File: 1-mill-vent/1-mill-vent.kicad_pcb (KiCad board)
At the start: 2 copper layers, 96.5 x 55.9 mm, 60 parts, among them J1 Differential:/Single, J3 No_Power_Control, J4 Front_panel_control, J5 Fan, J6 Ext Parts, J7 EXT Power Option, J8 POWER, Q1 2N3904, Q2 2N3904, Q3 2N3904, Q4 TSM480p06, U1 LM358, U2 LM78L05_TO92, U3 TSR_1-24120, U4 MPXV

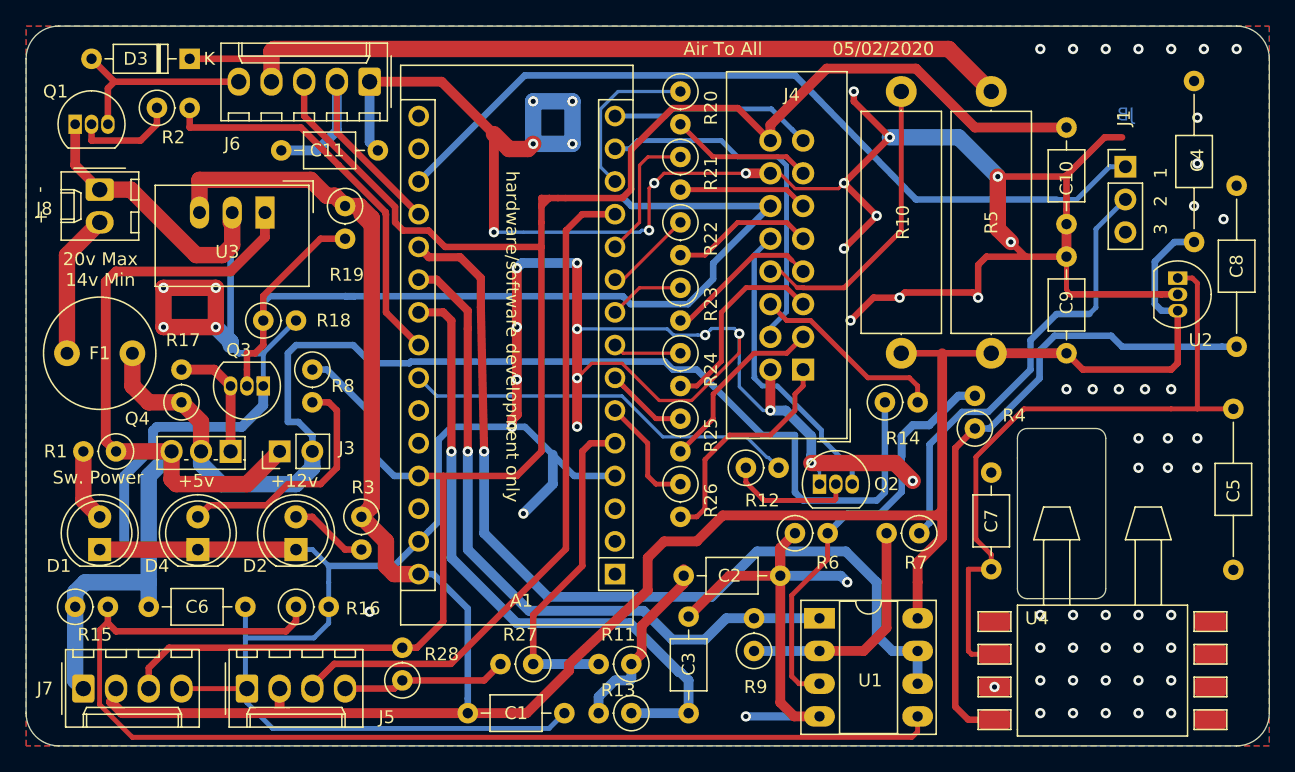
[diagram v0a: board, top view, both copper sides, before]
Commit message: Last update to ver1, start v2
V1 is first board
V2 is start of SMD design
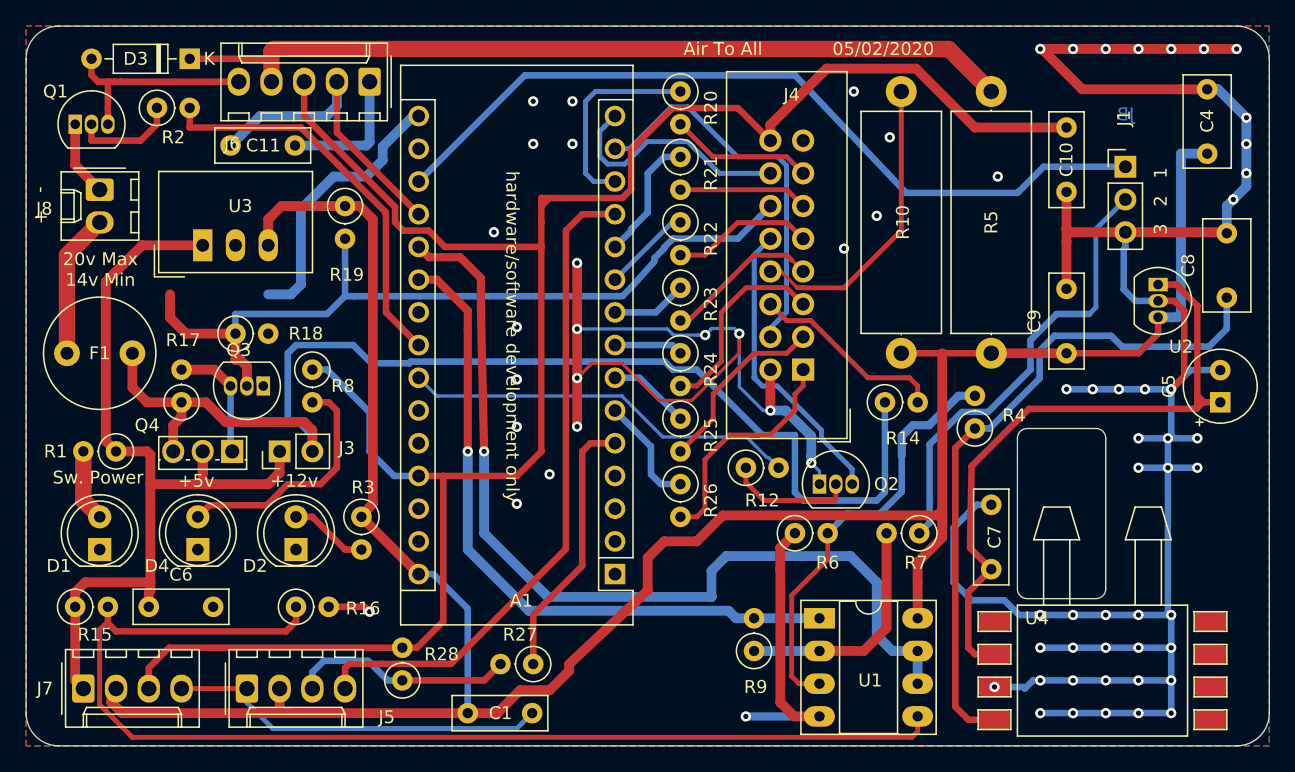
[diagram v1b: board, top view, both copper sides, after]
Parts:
- removed C2, C3: 0.1uF, Capacitor_THT:C_Axial_L3.8mm_D2.6mm_P7.50mm_Horizontal
- removed R11: 1k, Resistor_THT:R_Axial_DIN0207_L6.3mm_D2.5mm_P2.54mm_Vertical
- removed R13: 10k, Resistor_THT:R_Axial_DIN0207_L6.3mm_D2.5mm_P2.54mm_Vertical
- C1, C10, C11, C6, C7, C9: footprint Capacitor_THT:C_Axial_L3.8mm_D2.6mm_P7.50mm_Horizontal -> Capacitor_THT:C_Rect_L7.2mm_W2.5mm_P5.00mm_FKS2_FKP2_MKS2_MKP2
- C4, C8: footprint Capacitor_THT:C_Axial_L3.8mm_D2.6mm_P12.50mm_Horizontal -> Capacitor_THT:C_Rect_L7.0mm_W3.5mm_P5.00mm
- C5: footprint Capacitor_THT:C_Axial_L3.8mm_D2.6mm_P12.50mm_Horizontal -> Capacitor_THT:CP_Radial_Tantal_D5.5mm_P2.50mm
- F1: value 3A FB -> 2A FB
- Q4: value TSM480p06 -> TSM480P06CHX0G-Transistor_FET
- R7: value 10k -> 5k
- moved C4 6.93 mm to (183.1, 75.9)
- moved U3 5.45 mm to (105.2, 83.1), turned to 0 degrees
- moved C11 3.96 mm to (107.3, 75.3)
- moved C8 3.89 mm to (184.7, 87.1)
- moved R18 2.39 mm to (107.7, 89.9)
- moved U2 1.61 mm to (179.3, 86.1)
- moved C5 1.14 mm to (184.2, 95.2), turned to 90 degrees
- moved Q4 0.13 mm to (107.4, 99.1)
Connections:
- A1 pad 1: (no net) -> Net-(A1-Pad1)
- A1 pad 16: (no net) -> ON\*OFF
- A1 pad 17: (no net) -> Net-(A1-Pad17)
- A1 pad 2: (no net) -> Net-(A1-Pad2)
- A1 pad 22: RPM_V -> Net-(A1-Pad22)
- A1 pad 25: (no net) -> Net-(A1-Pad25)
- A1 pad 26: (no net) -> Net-(A1-Pad26)
- A1 pad 28: (no net) -> Net-(A1-Pad28)
- A1 pad 3: (no net) -> Net-(A1-Pad3)
- J4 pad 14: GND -> Down
- J4 pad 15: Down -> GND
- J5 pad 3: PWM -> Net-(J5-Pad3)
- J5 pad 4: Net-(J5-Pad4) -> PWM
- Q4 pad 2: Raw_Batt -> SW_Batt
- Q4 pad 3: SW_Batt -> Raw_Batt
- R27 pad 2: Net-(J5-Pad4) -> Net-(J5-Pad3)
- R28 pad 1: Net-(J5-Pad4) -> Net-(J5-Pad3)
- U4 pad 1: (no net) -> Net-(U4-Pad1)
- U4 pad 5: (no net) -> Net-(U4-Pad5)
- U4 pad 6: (no net) -> Net-(U4-Pad6)
- U4 pad 7: (no net) -> Net-(U4-Pad7)
- U4 pad 8: (no net) -> Net-(U4-Pad8)
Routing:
- net GND: track 467.1 -> 321.4 mm, vias 82 -> 68
- net RPM_V: track 50.6 -> 0.00 mm, vias 1 -> 0
- net Net-(J5-Pad3): track 0.00 -> 17.4 mm
- net Net-(C2-Pad1): track 14.6 -> 0.00 mm
- net Net-(J5-Pad4): track 12.9 -> 0.00 mm
- net ON\*OFF: track 74.0 -> 84.9 mm
- net Sensor_Power: track 52.5 -> 59.7 mm
- net +12V: track 195.1 -> 189.6 mm
- net RPM: track 26.0 -> 20.9 mm
- net SW_Batt: track 72.4 -> 67.4 mm
- net Down: track 15.9 -> 18.9 mm
- net LED7: track 12.9 -> 15.8 mm
- net Speed: track 22.3 -> 24.9 mm
- net Pressure: track 50.6 -> 52.8 mm
- net Up: track 28.2 -> 30.4 mm
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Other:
- board text added: "Gnd +5v +12v Sw. Batt"
- board text added: "PWM RPM +12v GND"
- board text removed: "RPM PWM +12v GND"
- board text removed: "Sw. Batt +12v +5v Gnd"
